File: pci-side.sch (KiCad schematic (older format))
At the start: 12 parts, among them J1 PCIE-064-02-F-D-TH, P1 5622-4100-ML, U1 SFW30R-2STE1LF

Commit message: rename board 1 files
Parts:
- C1, C2, C3: symbol CGA4F4X7T2W103M085AE:CGA4F4X7T2W103M085AE -> pci-side-rescue:CGA4F4X7T2W103M085AE-CGA4F4X7T2W103M085AE-m2-pcie4x-rescue
- D1, D2, D3: symbol 598-8010-107F:598-8010-107F -> pci-side-rescue:598-8010-107F-598-8010-107F-m2-pcie4x-rescue
- J1: symbol m2-pcie4x-rescue:PCIE-064-02-F-D-TH-PCIE-064-02-F-D-TH-Mini-ATX-PCIe-Extender-rescue -> pci-side-rescue:PCIE-064-02-F-D-TH-PCIE-064-02-F-D-TH-Mini-ATX-PCIe-Extender-rescue-m2-pcie4x-rescue
- P1: symbol 5622-4100-ML:5622-4100-ML -> pci-side-rescue:5622-4100-ML-5622-4100-ML-m2-pcie4x-rescue
- U1: symbol m2-pcie4x-rescue:SFW30R-2STE1LF-SFW30R-2STE1LF-Mini-ATX-PCIe-Extender-rescue -> pci-side-rescue:SFW30R-2STE1LF-SFW30R-2STE1LF-Mini-ATX-PCIe-Extender-rescue-m2-pcie4x-rescue
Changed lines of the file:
@@
 EESchema Schematic File Version 4
-LIBS:m2-pcie4x-cache
+LIBS:pci-side-cache
 EELAYER 29 0
 EELAYER END
@@
 	3250 3150 2700 3150
 $Comp
-L m2-pcie4x-rescue:PCIE-064-02-F-D-TH-PCIE-064-02-F-D-TH-Mini-ATX-PCIe-Extender-rescue J1
+L pci-side-rescue:PCIE-064-02-F-D-TH-PCIE-064-02-F-D-TH-Mini-ATX-PCIe-Extender-rescue-m2-pcie4x-rescue J1
 U 1 1 5D3C63FA
 P 4900 2300
@@
 $EndComp
 $Comp
-L m2-pcie4x-rescue:PCIE-064-02-F-D-TH-PCIE-064-02-F-D-TH-Mini-ATX-PCIe-Extender-rescue J1
+L pci-side-rescue:PCIE-064-02-F-D-TH-PCIE-064-02-F-D-TH-Mini-ATX-PCIe-Extender-rescue-m2-pcie4x-rescue J1
 U 2 1 5D3C7E7A
 P 2200 2350
@@
 CLKREQ#
 $Comp
-L 5622-4100-ML:5622-4100-ML P1
+L pci-side-rescue:5622-4100-ML-5622-4100-ML-m2-pcie4x-rescue P1
 U 1 1 5D5381C5
 P 2300 4950
@@
 Connection ~ 1300 5850
 $Comp
-L 598-8010-107F:598-8010-107F D1
+L pci-side-rescue:598-8010-107F-598-8010-107F-m2-pcie4x-rescue D1
 U 1 1 5D54D977
 P 3850 4000
@@
 $EndComp
 $Comp
-L 598-8010-107F:598-8010-107F D3
+L pci-side-rescue:598-8010-107F-598-8010-107F-m2-pcie4x-rescue D3
 U 1 1 5D54E55A
 P 3900 5000
@@
 $EndComp
 $Comp
-L 598-8010-107F:598-8010-107F D2
+L pci-side-rescue:598-8010-107F-598-8010-107F-m2-pcie4x-rescue D2
 U 1 1 5D54EE95
 P 3850 6150
@@
 $EndComp
 $Comp
-L CGA4F4X7T2W103M085AE:CGA4F4X7T2W103M085AE C1
+L pci-side-rescue:CGA4F4X7T2W103M085AE-CGA4F4X7T2W103M085AE-m2-pcie4x-rescue C1
 U 1 1 5D54FF0D
 P 5200 4200
@@
 $EndComp
 $Comp
-L CGA4F4X7T2W103M085AE:CGA4F4X7T2W103M085AE C2
+L pci-side-rescue:CGA4F4X7T2W103M085AE-CGA4F4X7T2W103M085AE-m2-pcie4x-rescue C2
 U 1 1 5D55449D
 P 5200 5200
@@
 $EndComp
 $Comp
-L CGA4F4X7T2W103M085AE:CGA4F4X7T2W103M085AE C3
+L pci-side-rescue:CGA4F4X7T2W103M085AE-CGA4F4X7T2W103M085AE-m2-pcie4x-rescue C3
 U 1 1 5D554DA0
 P 5200 6350
@@
 PER0+
 $Comp
-L m2-pcie4x-rescue:SFW30R-2STE1LF-SFW30R-2STE1LF-Mini-ATX-PCIe-Extender-rescue U1
+L pci-side-rescue:SFW30R-2STE1LF-SFW30R-2STE1LF-Mini-ATX-PCIe-Extender-rescue-m2-pcie4x-rescue U1
 U 1 1 5D413135
 P 7450 2200

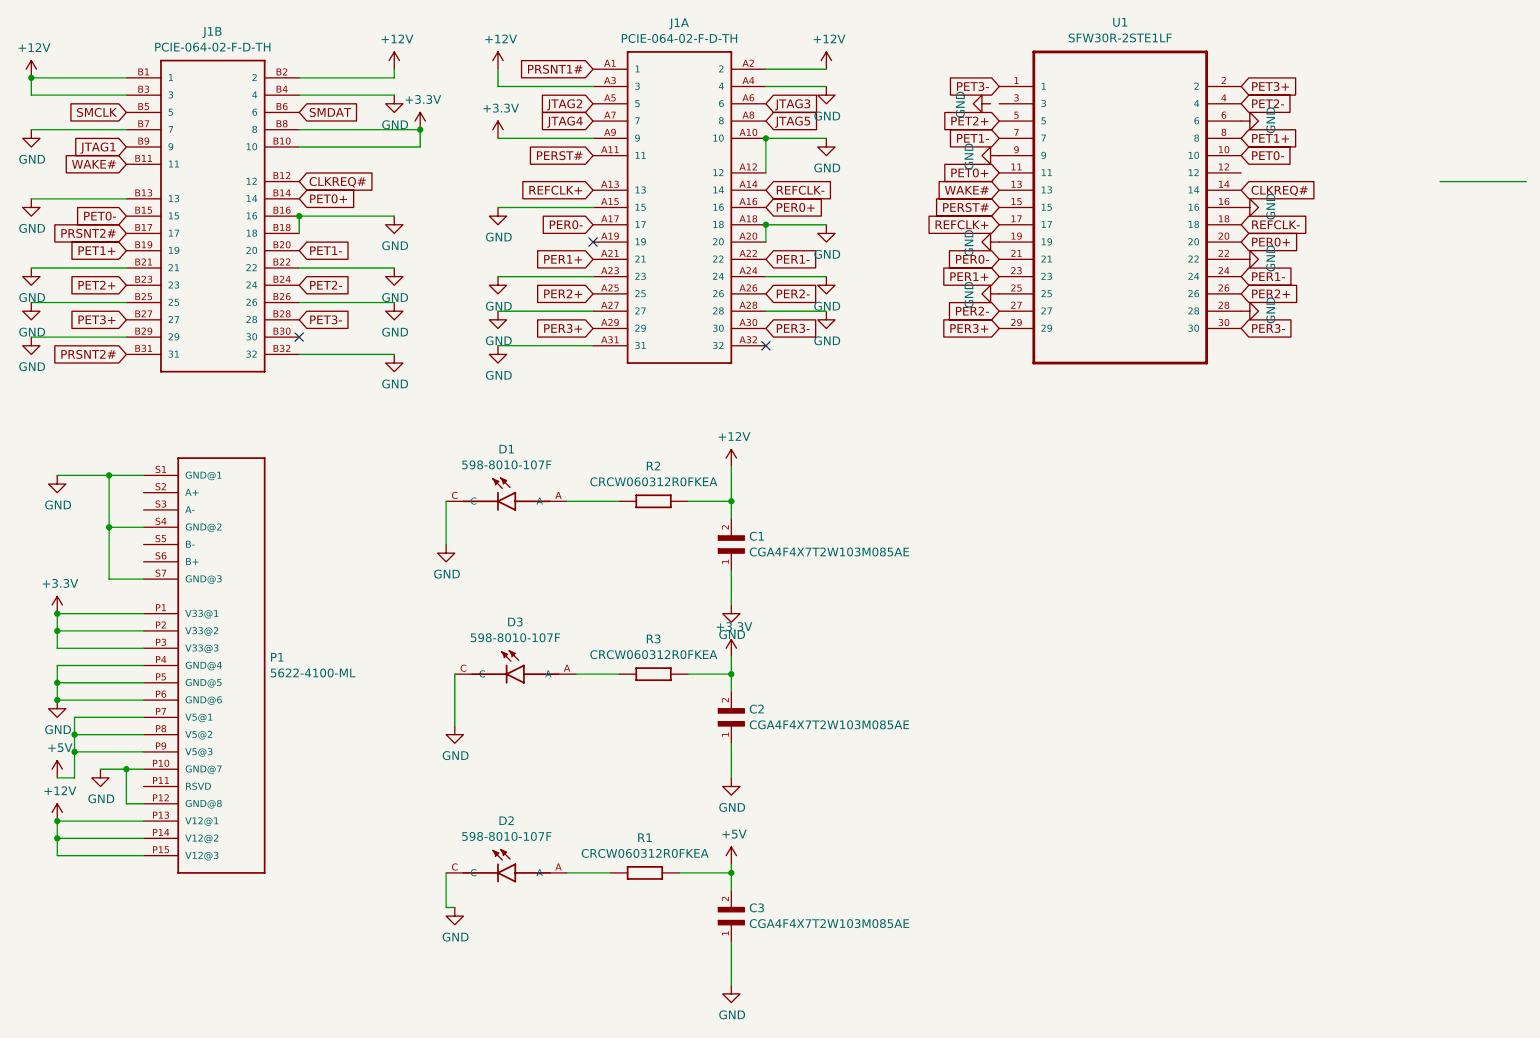
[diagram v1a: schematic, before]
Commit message: better dPair routing, follow spec, move svg
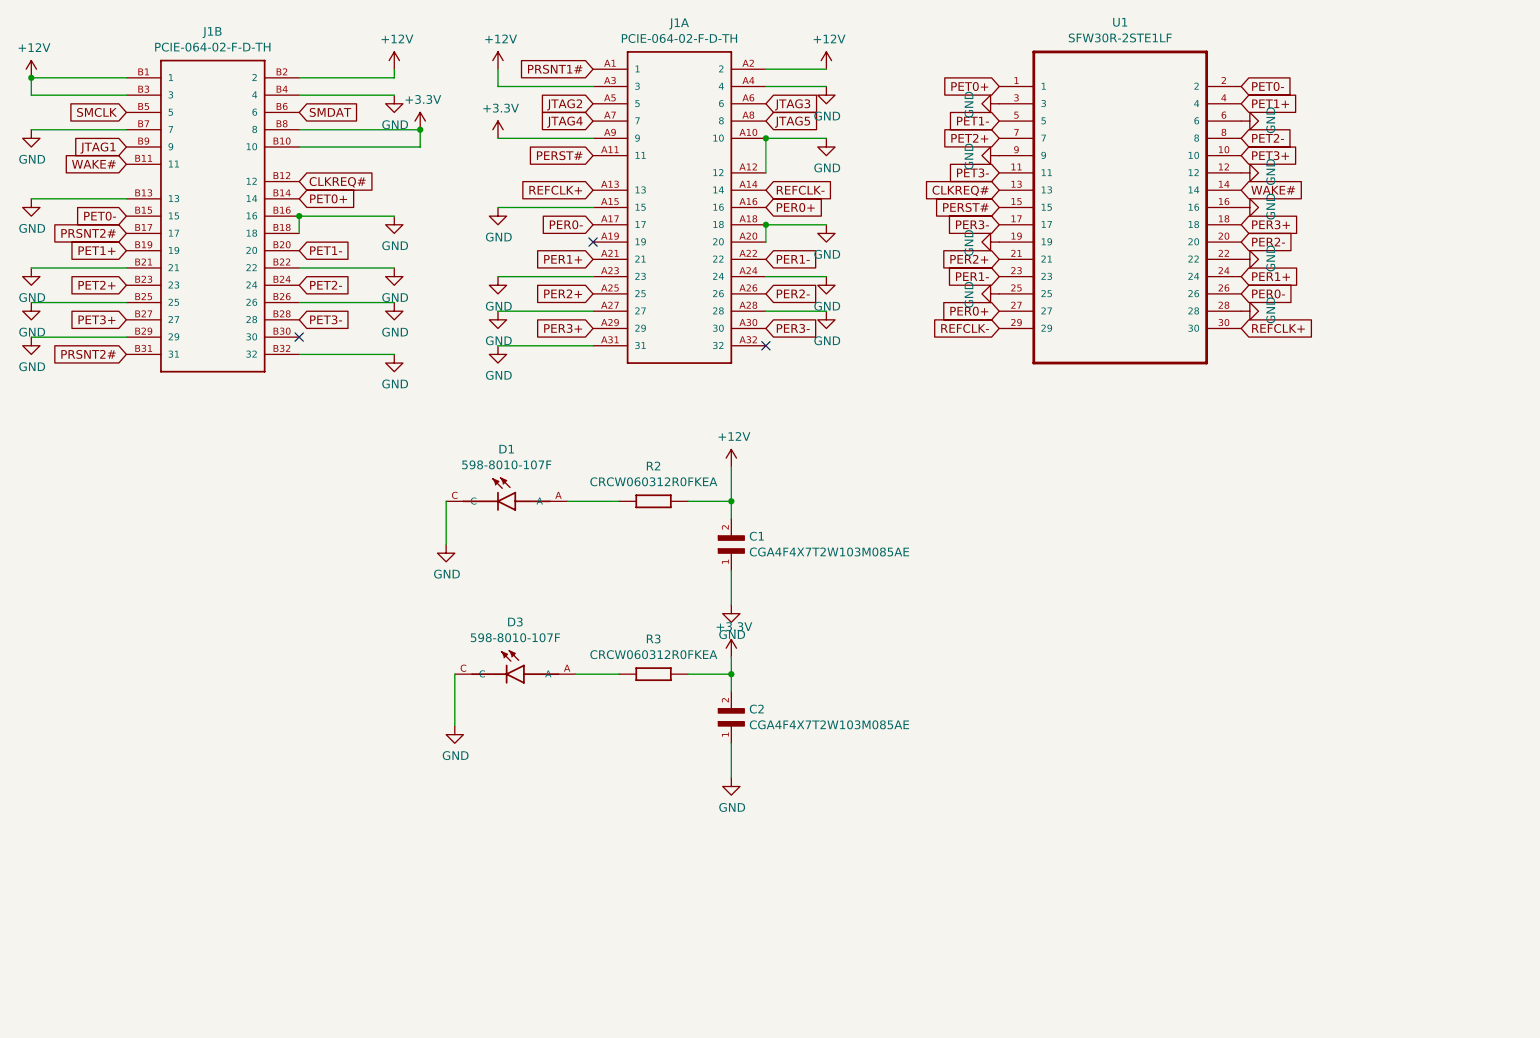
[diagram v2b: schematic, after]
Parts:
- removed C3: CGA4F4X7T2W103M085AE, CAPC2012X100N, symbol pci-side-rescue:CGA4F4X7T2W103M085AE-CGA4F4X7T2W103M085AE-m2-pcie4x-rescue
- removed D2: 598-8010-107F, LEDSC160X80X70L45N, symbol pci-side-rescue:598-8010-107F-598-8010-107F-m2-pcie4x-rescue
- removed P1: 5622-4100-ML, 3M_5622-4100-ML, symbol pci-side-rescue:5622-4100-ML-5622-4100-ML-m2-pcie4x-rescue
- removed R1: CRCW060312R0FKEA, 0603, symbol CRCW060312R0FKEA:CRCW060312R0FKEA
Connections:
- net CLKREQ#: now also U1.13; no longer U1.14
- net GND: now also U1.12, U1.3
- net PER0+: now also U1.27; no longer U1.20
- net PER0-: now also U1.26; no longer U1.21
- net PER1+: now also U1.24; no longer U1.23
- net PER1-: now also U1.23; no longer U1.24
- net PER2+: now also U1.21; no longer U1.26
- net PER2-: now also U1.20; no longer U1.27
- net PER3+: now also U1.18; no longer U1.29
- net PER3-: now also U1.17; no longer U1.30
- net PET0+: now also U1.1; no longer U1.11
- net PET0-: now also U1.2; no longer U1.10
- net PET1+: now also U1.4; no longer U1.8
- net PET1-: now also U1.5; no longer U1.7
- net PET2+: now also U1.7; no longer U1.5
- net PET2-: now also U1.8; no longer U1.4
- net PET3+: now also U1.10; no longer U1.2
- net PET3-: now also U1.11; no longer U1.1
- net REFCLK+: now also U1.30; no longer U1.17
- net REFCLK-: now also U1.29; no longer U1.18
- net WAKE#: now also U1.14; no longer U1.13
